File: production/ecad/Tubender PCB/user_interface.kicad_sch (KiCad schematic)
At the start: 97 parts, among them IC1 74HC4050D, IC2 RA8875L3N, IC3 CD4051BM96, IC4 CD4051BM96, J12 640387-2, J15 640387-2, J16 640387-2, J17 640387-2, J18 640387-2, J19 640387-2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

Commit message: small changes and reducing errors
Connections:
- net LEDK is gone; now on net GND: J7.1
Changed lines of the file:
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@@
 		)
 	)
-	(global_label "LEDK"
-		(shape input)
-		(at 48.26 49.53 0)
-		(fields_autoplaced yes)
-		(effects
-			(font
-				(size 1.27 1.27)
-			)
-			(justify left)
-		)
-		(property "Intersheetrefs" "${INTERSHEET_REFS}"
-			(at 55.9623 49.53 0)
-			(effects
-				(font
-					(size 1.27 1.27)
-				)
-				(justify left)
-				(hide yes)
-			)
-		)
-	)
 	(global_label "BUTTON_7"
 		(shape input)
@@
 					(unit 1)
 				)
+			)
+		)
+	)
+	(symbol
+		(lib_id "power:GND")
+		(at 48.26 49.53 90)
+		(unit 1)
+		(exclude_from_sim no)
+		(in_bom yes)
+		(on_board yes)
+		(dnp no)
+		(fields_autoplaced yes)
+		(property "Reference" "#PWR0218"
+			(at 54.61 49.53 0)
+			(effects
+				(font
+					(size 1.27 1.27)
+				)
+				(hide yes)
+			)
+		)
+		(property "Value" "GND"
+			(at 52.07 49.5299 90)
+			(effects
+				(font
+					(size 1.27 1.27)
+				)
+				(justify right)
+			)
+		)
+		(property "Footprint" ""
+			(at 48.26 49.53 0)
+			(effects
+				(font
+					(size 1.27 1.27)
+				)
+				(hide yes)
+			)
+		)
+		(property "Datasheet" ""
+			(at 48.26 49.53 0)
+			(effects
+				(font
+					(size 1.27 1.27)
+				)
+				(hide yes)
+			)
+		)
+		(property "Description" "Power symbol creates a global label with name \"GND\" , ground"
+			(at 48.26 49.53 0)
+			(effects
+				(font
+					(size 1.27 1.27)
+				)
+				(hide yes)
+			)
+		)
+		(pin "1"
+		)
+		(instances
+			(project ""
+				(path "/3e1aedd0-6089-4edb-92c7-0c31da2e7927/3052d7ff-6484-4cba-b320-c154d511606f"
+					(reference "#PWR0218")
+					(unit 1)
+				)

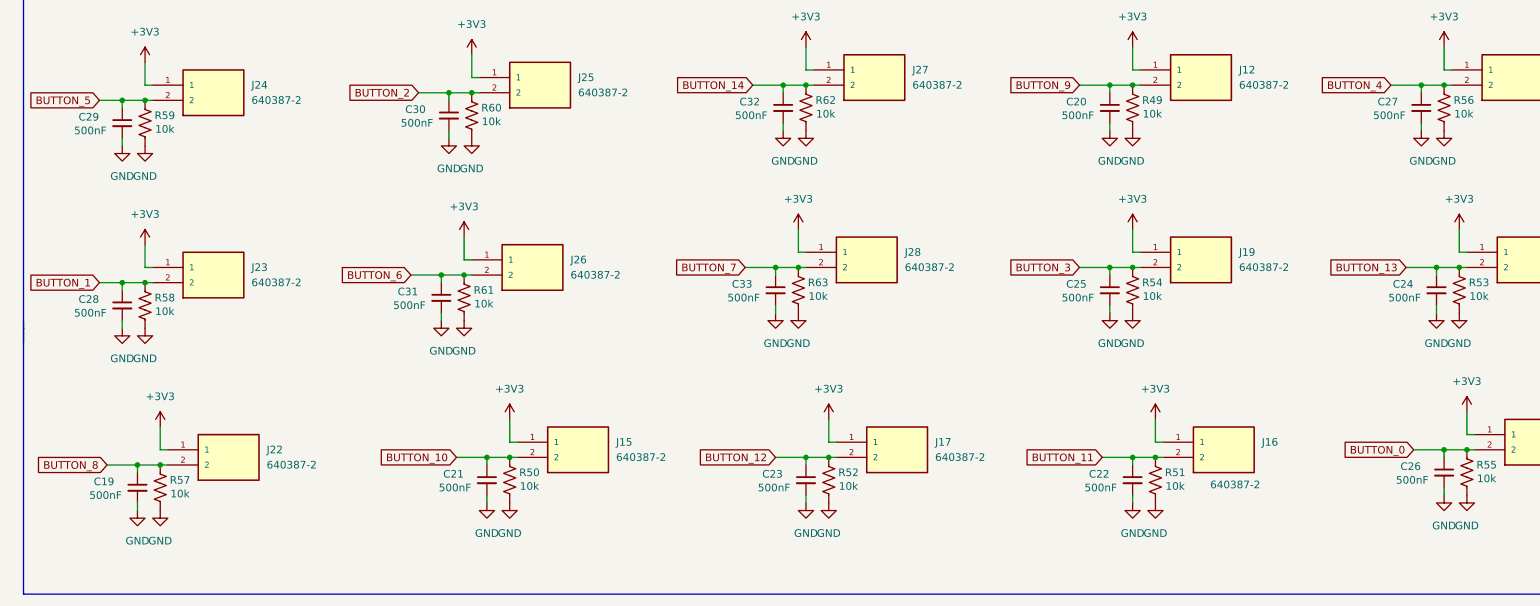
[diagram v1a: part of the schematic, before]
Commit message: Fixed RC Cap Value
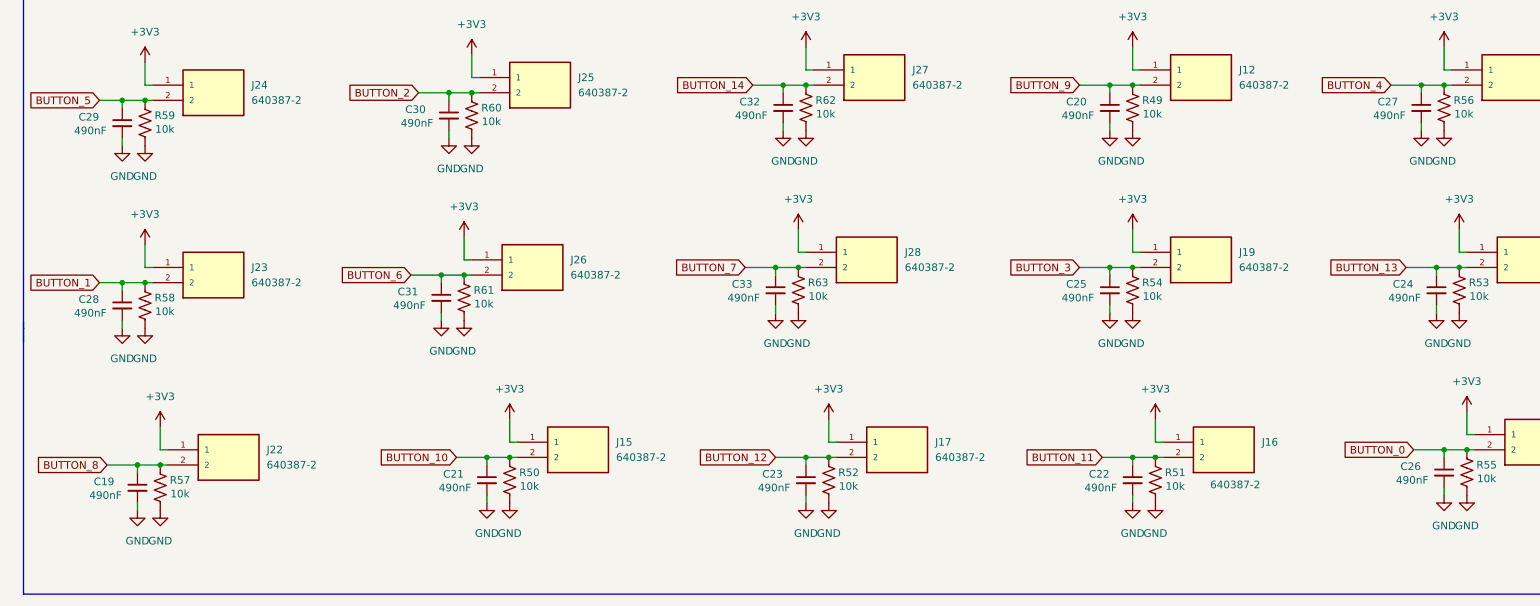
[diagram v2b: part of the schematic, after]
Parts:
- C19, C20, C21, C22, C23, C24, C25, C26, C27, C28, C29, C30, C31, C32, C33: value 500nF -> 490nF
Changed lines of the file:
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@@
 			)
 		)
-		(property "Value" "500nF"
+		(property "Value" "490nF"
 			(at 256.286 231.14 0)
 			(effects
@@
 			)
 		)
-		(property "Value" "500nF"
+		(property "Value" "490nF"
 			(at 36.576 203.2 0)
 			(effects
@@
 			)
 		)
-		(property "Value" "500nF"
+		(property "Value" "490nF"
 			(at 97.536 262.89 0)
 			(effects
@@
 			)
 		)
-		(property "Value" "500nF"
+		(property "Value" "490nF"
 			(at 201.676 200.66 0)
 			(effects
@@
 			)
 		)
-		(property "Value" "500nF"
+		(property "Value" "490nF"
 			(at 91.186 201.93 0)
 			(effects
@@
 			)
 		)
-		(property "Value" "500nF"
+		(property "Value" "490nF"
 			(at 89.916 232.41 0)
 			(effects
@@
 			)
 		)
-		(property "Value" "500nF"
+		(property "Value" "490nF"
 			(at 257.556 261.62 0)
 			(effects
@@
 			)
 		)
-		(property "Value" "500nF"
+		(property "Value" "490nF"
 			(at 253.746 200.66 0)
 			(effects
@@
 			)
 		)
-		(property "Value" "500nF"
+		(property "Value" "490nF"
 			(at 145.796 231.14 0)
 			(effects
@@
 			)
 		)
-		(property "Value" "500nF"
+		(property "Value" "490nF"
 			(at 147.066 200.66 0)
 			(effects
@@
 			)
 		)
-		(property "Value" "500nF"
+		(property "Value" "490nF"
 			(at 36.576 233.68 0)
 			(effects
@@
 			)
 		)
-		(property "Value" "500nF"
+		(property "Value" "490nF"
 			(at 39.116 264.16 0)
 			(effects
@@
 			)
 		)
-		(property "Value" "500nF"
+		(property "Value" "490nF"
 			(at 150.876 262.89 0)
 			(effects
@@
 			)
 		)
-		(property "Value" "500nF"
+		(property "Value" "490nF"
 			(at 205.486 262.89 0)
 			(effects
@@
 			)
 		)
-		(property "Value" "500nF"
+		(property "Value" "490nF"
 			(at 201.676 231.14 0)
 			(effects

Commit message: replaced and rewired IC2
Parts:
- IC2: footprint ${KIPRJMOD}:QFP40P1600X1600X160-128N -> ${KIPRJMOD}:QFP50P1600X1600X160-100N
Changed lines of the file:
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@@
 			)
 		)
-		(property "Footprint" "${KIPRJMOD}:QFP40P1600X1600X160-128N"
+		(property "Footprint" "${KIPRJMOD}:QFP50P1600X1600X160-100N"
 			(at 231.14 143.18 0)
 			(effects
